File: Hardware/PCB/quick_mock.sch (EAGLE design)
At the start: 24 parts

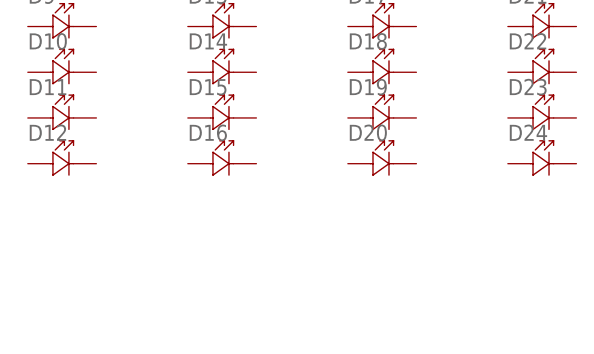
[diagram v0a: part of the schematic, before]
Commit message: adjust hole sizes. replace emitter LEDs
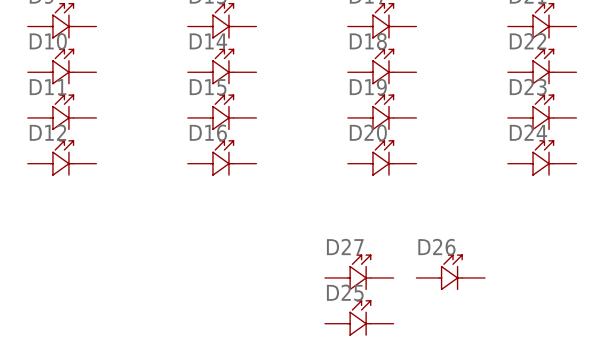
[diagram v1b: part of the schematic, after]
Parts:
- added D25, D27: VSMB2020X01, Rob-Diodes:VSMB2020X01
- added D26: LED-603, Rob-Diodes:LED-603
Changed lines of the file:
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@@
 <part name="D23" library="Rob-Diodes" library_urn="urn:adsk.eagle:library:37150039" deviceset="LED" device="-603" package3d_urn="urn:adsk.eagle:package:37041000/3"/>
 <part name="D24" library="Rob-Diodes" library_urn="urn:adsk.eagle:library:37150039" deviceset="LED" device="-603" package3d_urn="urn:adsk.eagle:package:37041000/3"/>
+<part name="D25" library="Rob-Diodes" library_urn="urn:adsk.eagle:library:37150039" deviceset="VSMB2020X01" device="" package3d_urn="urn:adsk.eagle:package:39410737/2"/>
+<part name="D26" library="Rob-Diodes" library_urn="urn:adsk.eagle:library:37150039" deviceset="LED" device="-603" package3d_urn="urn:adsk.eagle:package:37041000/3"/>
+<part name="D27" library="Rob-Diodes" library_urn="urn:adsk.eagle:library:37150039" deviceset="VSMB2020X01" device="" package3d_urn="urn:adsk.eagle:package:39410737/2"/>
 </parts>
 <sheets>
@@
 <attribute name="NAME" x="96.52" y="5.08" size="1.778" layer="95" font="vector"/>
 </instance>
+<instance part="D25" gate="G$1" x="78.74" y="-15.24" smashed="yes">
+<attribute name="NAME" x="76.2" y="-12.7" size="1.778" layer="95" font="vector"/>
+</instance>
+<instance part="D26" gate="G$1" x="88.9" y="-10.16" smashed="yes">
+<attribute name="NAME" x="86.36" y="-7.62" size="1.778" layer="95" font="vector"/>
+</instance>
+<instance part="D27" gate="G$1" x="78.74" y="-10.16" smashed="yes">
+<attribute name="NAME" x="76.2" y="-7.62" size="1.778" layer="95" font="vector"/>
+</instance>
 </instances>

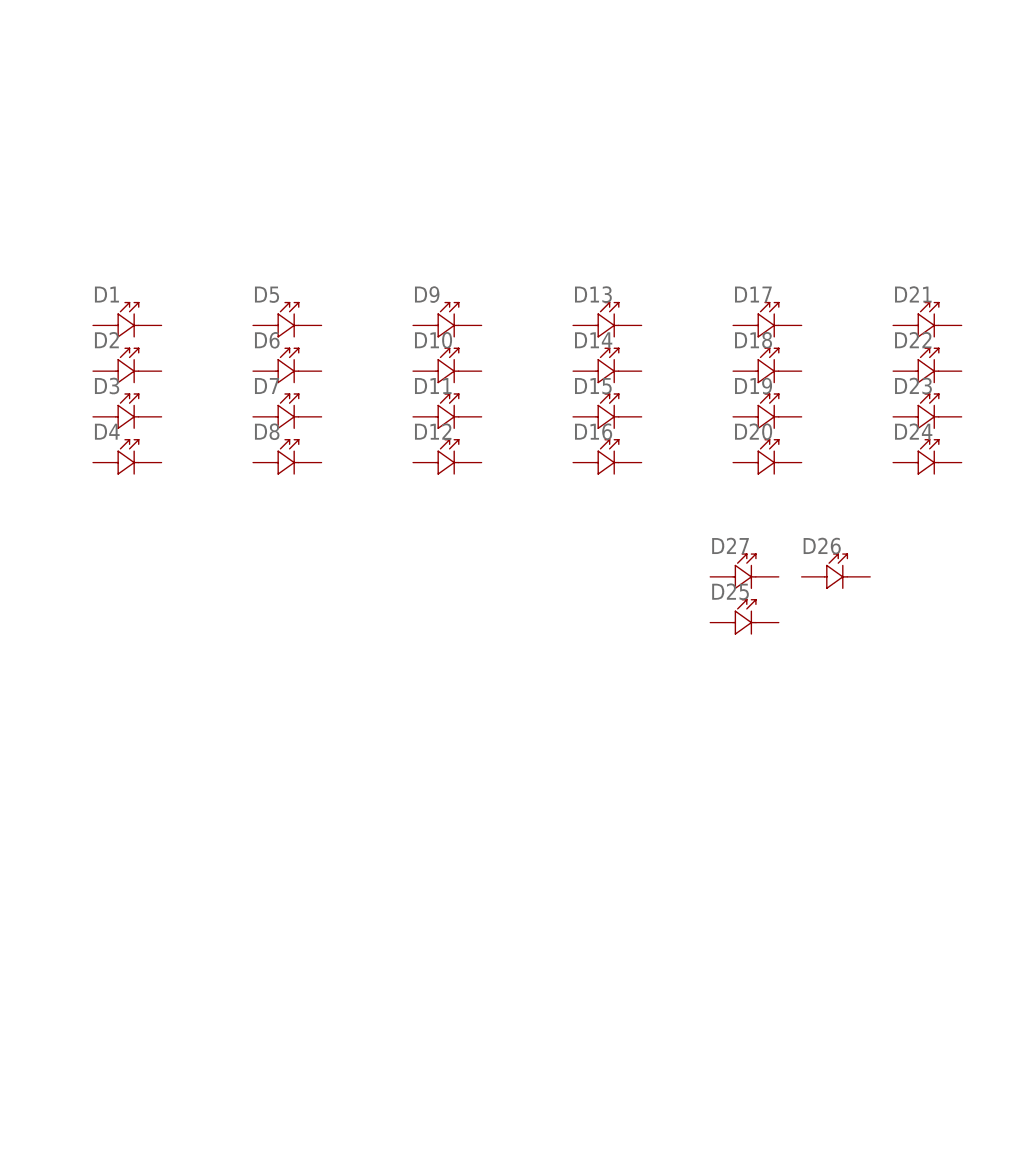
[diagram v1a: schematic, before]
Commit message: move switches. add two types of lanyard mounting
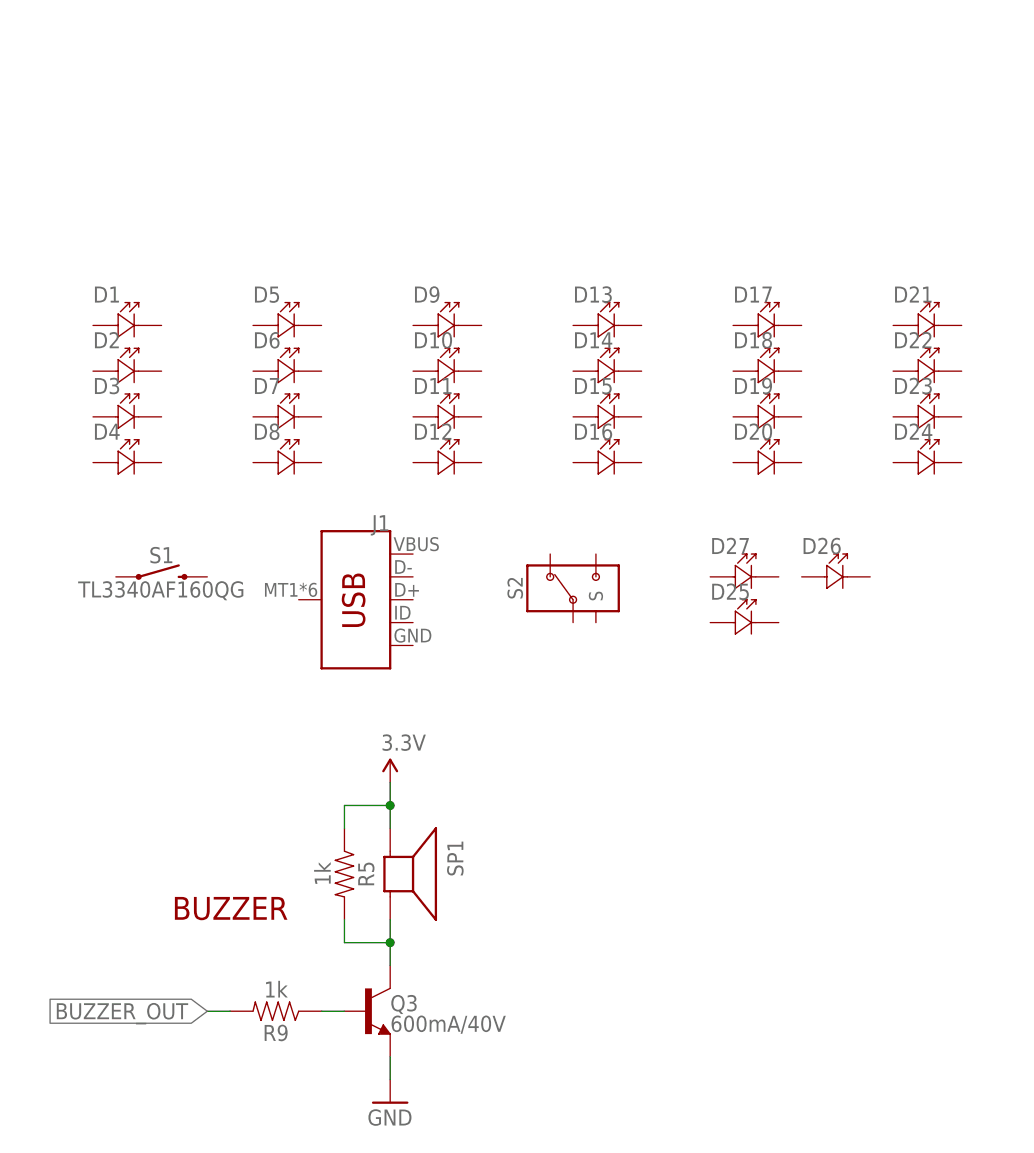
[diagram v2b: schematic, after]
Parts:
- added J1: (no value), SparkFun-Connectors-new:USB_MICRO-B
- added Q3: 600mA/40V, SparkFun-DiscreteSemi:TRANS_NPN-MMBT2222AL
- added R5, R9: 1k, SparkFun-Resistors:10KOHM-0603-1/10W-1%
- added S1: TL3340AF160QG, Rob-Switches:TL3340AF160QG
- added S2: CUS-12B, IDEO-Switches:CUS-12B
- added SP1: SPEAKER/PS12, adafruit:SPEAKER/PS12
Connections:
- new net 3.3V: R5.1, SP1.+
- new net BUZZER_OUT: R9.2
- new net GND: Q3.E
- new net N$26: Q3.B, R9.1
- new net N$3: Q3.C, R5.2, SP1.-
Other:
- note added: "BUZZER"
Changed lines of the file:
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@@
 <layer number="2" name="Route2" color="1" fill="3" visible="no" active="no"/>
 <layer number="3" name="Route3" color="4" fill="3" visible="no" active="no"/>
+<layer number="4" name="Route4" color="1" fill="4" visible="no" active="no"/>
+<layer number="5" name="Route5" color="4" fill="4" visible="no" active="no"/>
+<layer number="6" name="Route6" color="1" fill="8" visible="no" active="no"/>
+<layer number="7" name="Route7" color="4" fill="8" visible="no" active="no"/>
+<layer number="8" name="Route8" color="1" fill="2" visible="no" active="no"/>
+<layer number="9" name="Route9" color="4" fill="2" visible="no" active="no"/>
+<layer number="10" name="Route10" color="1" fill="7" visible="no" active="no"/>
+<layer number="11" name="Route11" color="4" fill="7" visible="no" active="no"/>
+<layer number="12" name="Route12" color="1" fill="5" visible="no" active="no"/>
+<layer number="13" name="Route13" color="4" fill="5" visible="no" active="no"/>
 <layer number="14" name="Route14" color="1" fill="6" visible="no" active="no"/>
 <layer number="15" name="Route15" color="4" fill="6" visible="no" active="no"/>
@@
 <layer number="115" name="ReferenceISLANDS" color="7" fill="1" visible="yes" active="yes"/>
 <layer number="116" name="Patch_BOT" color="9" fill="4" visible="yes" active="yes"/>
+<layer number="117" name="art" color="7" fill="1" visible="yes" active="yes"/>
 <layer number="118" name="Rect_Pads" color="7" fill="1" visible="yes" active="yes"/>
+<layer number="119" name="Bot_pads" color="1" fill="1" visible="yes" active="yes"/>
+<layer number="120" name="art2" color="7" fill="1" visible="yes" active="yes"/>
 <layer number="121" name="_tsilk" color="7" fill="1" visible="yes" active="yes"/>
 <layer number="122" name="_bsilk" color="7" fill="1" visible="yes" active="yes"/>
@@
 <layer number="128" name="_bValues" color="7" fill="1" visible="yes" active="yes"/>
 <layer number="129" name="Mask" color="7" fill="1" visible="yes" active="yes"/>
+<layer number="130" name="art3" color="7" fill="1" visible="yes" active="yes"/>
 <layer number="131" name="tAdjust" color="7" fill="1" visible="yes" active="yes"/>
 <layer number="132" name="bAdjust" color="7" fill="1" visible="yes" active="yes"/>
@@
 <layer number="230" name="230bmp" color="7" fill="1" visible="yes" active="yes"/>
 <layer number="231" name="231bmp" color="7" fill="1" visible="yes" active="yes"/>
+<layer number="232" name="Eagle3D_PG2" color="7" fill="1" visible="no" active="no"/>
+<layer number="233" name="Eagle3D_PG3" color="7" fill="1" visible="no" active="no"/>
 <layer number="248" name="Housing" color="7" fill="1" visible="yes" active="yes"/>
 <layer number="249" name="Edge" color="7" fill="1" visible="yes" active="yes"/>
@@
 <part name="D26" library="Rob-Diodes" library_urn="urn:adsk.eagle:library:37150039" deviceset="LED" device="-603" package3d_urn="urn:adsk.eagle:package:37041000/3"/>
 <part name="D27" library="Rob-Diodes" library_urn="urn:adsk.eagle:library:37150039" deviceset="VSMB2020X01" device="" package3d_urn="urn:adsk.eagle:package:39410737/2"/>
+<part name="S2" library="IDEO-Switches" deviceset="CUS-12B" device="" override_package3d_urn="urn:adsk.eagle:package:39505090/2" override_package_urn="urn:adsk.eagle:footprint:39505091/1"/>
+<part name="J1" library="SparkFun-Connectors-new" deviceset="USB_MICRO-B" device="" override_package3d_urn="urn:adsk.eagle:package:39505002/4" override_package_urn="urn:adsk.eagle:footprint:39505003/1"/>
+<part name="S1" library="Rob-Switches" library_urn="urn:adsk.eagle:library:39524603" deviceset="TL3340AF160QG" device="" package3d_urn="urn:adsk.eagle:package:39524606/4"/>
+<part name="Q3" library="SparkFun-DiscreteSemi" deviceset="TRANS_NPN" device="-MMBT2222AL" value="600mA/40V"/>
+<part name="SUPPLY17" library="SparkFun-Aesthetics" deviceset="3.3V" device=""/>
+<part name="R9" library="SparkFun-Resistors" deviceset="10KOHM" device="-0603-1/10W-1%" value="1k"/>
+<part name="GND38" library="SparkFun" deviceset="GND" device=""/>
+<part name="R5" library="SparkFun-Resistors" deviceset="10KOHM" device="-0603-1/10W-1%" value="1k"/>
+<part name="SP1" library="adafruit" deviceset="SPEAKER" device="/PS12" override_package3d_urn="urn:adsk.eagle:package:39544791/3" override_package_urn="urn:adsk.eagle:footprint:39544792/1"/>
 </parts>
 <sheets>
 <sheet>
 <plain>
+<text x="22.86" y="-48.26" size="2.54" layer="94" align="bottom-center">BUZZER</text>
 </plain>
 <instances>
@@
 <attribute name="NAME" x="76.2" y="-7.62" size="1.778" layer="95" font="vector"/>
 </instance>
+<instance part="S2" gate="G$1" x="60.96" y="-10.16" smashed="yes" rot="R90">
+<attribute name="NAME" x="55.372" y="-12.7" size="1.6764" layer="95" font="vector" ratio="10" rot="R90"/>
+</instance>
+<instance part="J1" gate="G$1" x="38.1" y="-12.7" smashed="yes" rot="MR0">
+<attribute name="VALUE" x="40.64" y="-20.574" size="1.778" layer="96" font="vector" rot="MR0" align="top-left"/>
+<attribute name="NAME" x="40.64" y="-5.08" size="1.778" layer="95" font="vector" rot="MR0"/>
+</instance>
+<instance part="S1" gate="G$1" x="12.7" y="-10.16" smashed="yes">
+<attribute name="NAME" x="15.24" y="-8.636" size="1.778" layer="95" font="vector" align="bottom-center"/>
+<attribute name="VALUE" x="15.24" y="-10.668" size="1.778" layer="96" font="vector" align="top-center"/>
+</instance>
+<instance part="Q3" gate="G$1" x="38.1" y="-58.42" smashed="yes">
+<attribute name="NAME" x="40.64" y="-58.42" size="1.778" layer="95" font="vector"/>
+<attribute name="VALUE" x="40.64" y="-60.706" size="1.778" layer="96" font="vector"/>
+</instance>
+<instance part="SUPPLY17" gate="G$1" x="40.64" y="-33.02" smashed="yes">
+<attribute name="VALUE" x="39.624" y="-29.464" size="1.778" layer="96"/>
+</instance>
+<instance part="R9" gate="G$1" x="27.94" y="-58.42" smashed="yes" rot="R180">
+<attribute name="NAME" x="27.94" y="-59.944" size="1.778" layer="95" font="vector" rot="R180" align="bottom-center"/>
+<attribute name="VALUE" x="27.94" y="-56.896" size="1.778" layer="96" font="vector" rot="R180" align="top-center"/>
+</instance>
+<instance part="GND38" gate="1" x="40.64" y="-68.58" smashed="yes">
+<attribute name="VALUE" x="38.1" y="-71.12" size="1.778" layer="96"/>
+</instance>
+<instance part="R5" gate="G$1" x="35.56" y="-43.18" smashed="yes" rot="R270">
+<attribute name="NAME" x="37.084" y="-43.18" size="1.778" layer="95" font="vector" rot="R270" align="bottom-center"/>
+<attribute name="VALUE" x="34.036" y="-43.18" size="1.778" layer="96" font="vector" rot="R270" align="top-center"/>
+</instance>
+<instance part="SP1" gate="S1" x="40.64" y="-43.18" smashed="yes" rot="R270">
+<attribute name="NAME" x="46.99" y="-39.37" size="1.778" layer="95" rot="R270"/>
+</instance>
 </instances>
 <busses>
 </busses>
 <nets>
+<net name="GND" class="0">
+<segment>
+<pinref part="Q3" gate="G$1" pin="E"/>
+<pinref part="GND38" gate="1" pin="GND"/>
+<wire x1="40.64" y1="-63.5" x2="40.64" y2="-66.04" width="0.1524" layer="91"/>
+</segment>
+</net>
+<net name="3.3V" class="0">
+<segment>
+<pinref part="SUPPLY17" gate="G$1" pin="3.3V"/>
+<wire x1="40.64" y1="-33.02" x2="40.64" y2="-35.56" width="0.1524" layer="91"/>
+<pinref part="R5" gate="G$1" pin="1"/>
+<wire x1="35.56" y1="-38.1" x2="35.56" y2="-35.56" width="0.1524" layer="91"/>
+<wire x1="35.56" y1="-35.56" x2="40.64" y2="-35.56" width="0.1524" layer="91"/>
+<pinref part="SP1" gate="S1" pin="+"/>
+<wire x1="40.64" y1="-35.56" x2="40.64" y2="-38.1" width="0.1524" layer="91"/>
+<junction x="40.64" y="-35.56"/>
+</segment>
+</net>
+<net name="BUZZER_OUT" class="0">
+<segment>
+<pinref part="R9" gate="G$1" pin="2"/>
+<wire x1="20.32" y1="-58.42" x2="22.86" y2="-58.42" width="0.1524" layer="91"/>
+<label x="20.32" y="-58.42" size="1.778" layer="95" rot="R180" xref="yes"/>
+</segment>
+</net>
+<net name="N$26" class="0">
+<segment>
+<pinref part="R9" gate="G$1" pin="1"/>
+<pinref part="Q3" gate="G$1" pin="B"/>
+<wire x1="33.02" y1="-58.42" x2="35.56" y2="-58.42" width="0.1524" layer="91"/>
+</segment>
+</net>
+<net name="N$3" class="0">
+<segment>
+<pinref part="R5" gate="G$1" pin="2"/>
+<wire x1="35.56" y1="-48.26" x2="35.56" y2="-50.8" width="0.1524" layer="91"/>
+<wire x1="35.56" y1="-50.8" x2="40.64" y2="-50.8" width="0.1524" layer="91"/>
+<pinref part="Q3" gate="G$1" pin="C"/>
+<wire x1="40.64" y1="-50.8" x2="40.64" y2="-53.34" width="0.1524" layer="91"/>
+<pinref part="SP1" gate="S1" pin="-"/>
+<wire x1="40.64" y1="-50.8" x2="40.64" y2="-48.26" width="0.1524" layer="91"/>
+<junction x="40.64" y="-50.8"/>
+</segment>
+</net>
 </nets>
 </sheet>
@@
 packages will not be understood (or retained) with this version.
 </note>
+<note version="9.4" severity="warning">
+Since Version 9.4, EAGLE supports the overriding of 3D packages
+in schematics and board files. Those overridden 3d packages
+will not be understood (or retained) with this version.
+</note>
 </compatibility>

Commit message: adjust lanyard holes. prep mock PCB for fab.
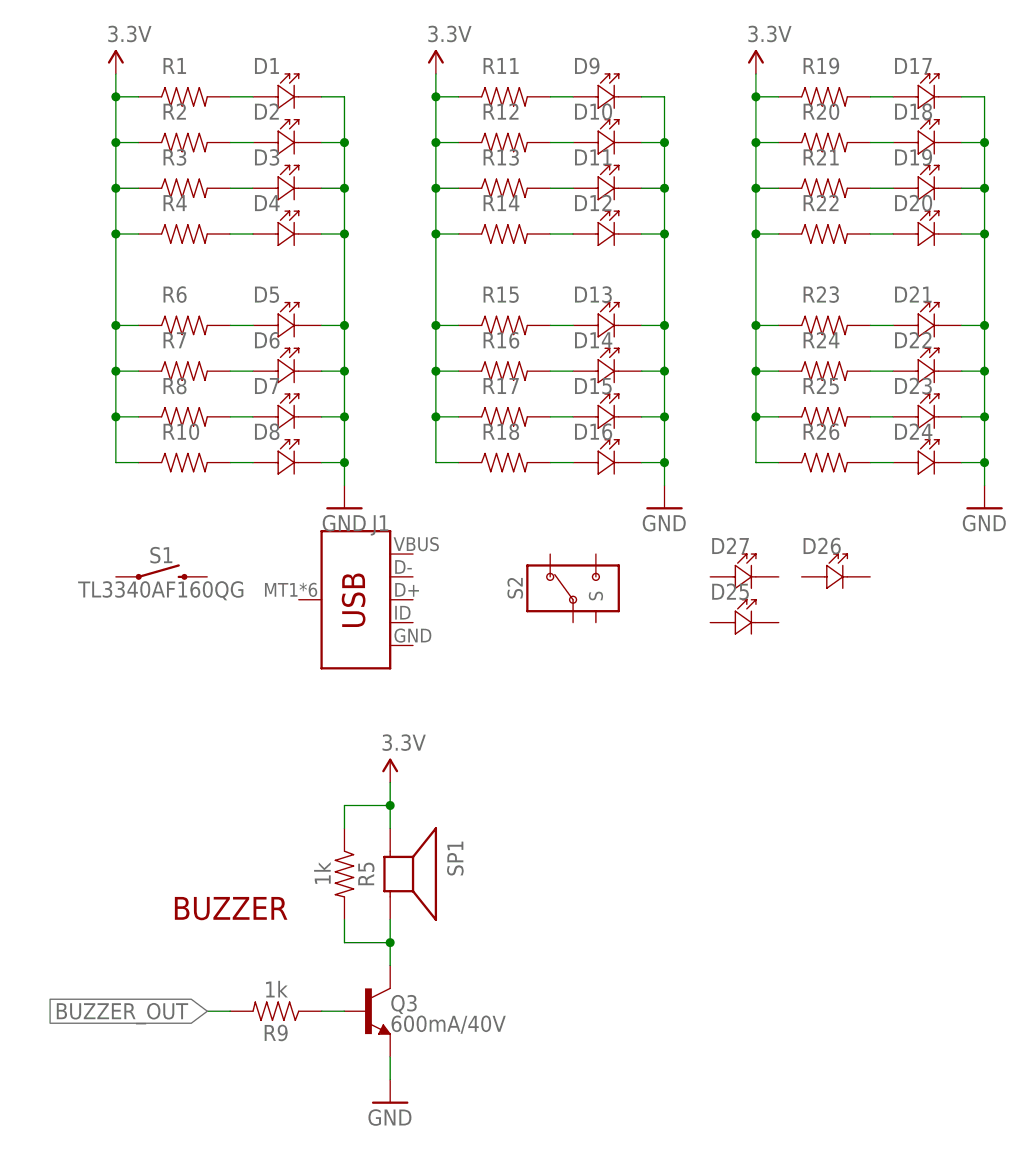
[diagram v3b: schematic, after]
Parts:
- added R1, R10, R11, R12, R13, R14, R15, R16, R17, R18, R19, R2, R20, R21, R22, R23, R24, R25, R26, R3, R4, R6, R7, R8: (no value), Rob-Resistors:RESISTOR-603
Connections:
- new net N$1: D1.ANODE+, R1.2
- new net N$14: D9.ANODE+, R11.2
- new net N$15: D10.ANODE+, R12.2
- new net N$16: D11.ANODE+, R13.2
- new net N$17: D12.ANODE+, R14.2
- new net N$18: D13.ANODE+, R15.2
- new net N$19: D14.ANODE+, R16.2
- new net N$2: D2.ANODE+, R2.2
- new net N$20: D15.ANODE+, R17.2
- new net N$21: D16.ANODE+, R18.2
- new net N$22: D24.ANODE+, R26.2
- new net N$23: D23.ANODE+, R25.2
- new net N$24: D22.ANODE+, R24.2
- new net N$25: D21.ANODE+, R23.2
- new net N$27: D20.ANODE+, R22.2
- new net N$28: D19.ANODE+, R21.2
- new net N$29: D18.ANODE+, R20.2
- new net N$30: D17.ANODE+, R19.2
- new net N$4: D3.ANODE+, R3.2
- new net N$5: D4.ANODE+, R4.2
- new net N$6: D5.ANODE+, R6.2
- new net N$7: D6.ANODE+, R7.2
- new net N$8: D7.ANODE+, R8.2
- new net N$9: D8.ANODE+, R10.2
- net 3.3V: now also R1.1, R10.1, R11.1, R12.1, R13.1, R14.1, R15.1, R16.1, R17.1, R18.1, R19.1, R2.1, R20.1, R21.1, R22.1, R23.1, R24.1, R25.1, R26.1, R3.1, R4.1, R6.1, R7.1, R8.1
- net GND: now also D1.CATHODE-, D10.CATHODE-, D11.CATHODE-, D12.CATHODE-, D13.CATHODE-, D14.CATHODE-, D15.CATHODE-, D16.CATHODE-, D17.CATHODE-, D18.CATHODE-, D19.CATHODE-, D2.CATHODE-, D20.CATHODE-, D21.CATHODE-, D22.CATHODE-, D23.CATHODE-, D24.CATHODE-, D3.CATHODE-, D4.CATHODE-, D5.CATHODE-, D6.CATHODE-, D7.CATHODE-, D8.CATHODE-, D9.CATHODE-
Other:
- moved on the sheet: D1, D10, D11, D12, D17, D18, D19, D2, D20, D3, D4, D9
